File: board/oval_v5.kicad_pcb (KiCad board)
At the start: 2 copper layers, 100 x 60 mm, 143 parts, among them J1 HDR-5x1, J10 HDR-4x1, J11 HDR-4x1, J12 HDR-4x1, J13 HDR-4x1, J14 HDR-4x1, J15 HDR-4x1, J16 HDR-4x1, J17 HDR-4x1, J18 Conn_Coaxial, J19 Conn_01x02, J2 HDR-4x1, J20 Conn_01x02, J21 Conn_02x02_Counter_Clockwise, J22 HDR-2x1, J23 HDR-2x1, J25 Conn_01x06, J3 HDR-4x1, J4 Conn_01x06, J5 Micro_SD_Card, J6 Conn_01x02, J7 HDR-4x1, J8 Conn_01x08, J9 HDR-4x1, P1 USB_C_Plug_USB2.0, Q1 Q_PMOS_GSD, Q2 MMBT3904, Q3 MMBT3904, SW1 SW_DIP_x02, SW2 SW_DIP_x02, U1 RV-8803, U10 SiP32431DR3, U11 SiP32431DR3, U12 SiP32431DR3, U13 SiP32431DR3, U14 SiP32431DR3, U16 PCA9548APW, U17 SiP32431DR3, U18 PCA9555PW, U2 ESP32-S3-WROOM-1, U3 TMP117xxDRV, U4 RFM95W-915S2, U7 MAX3485, U8 AP7361C-33E, U9 AP7361C-33E

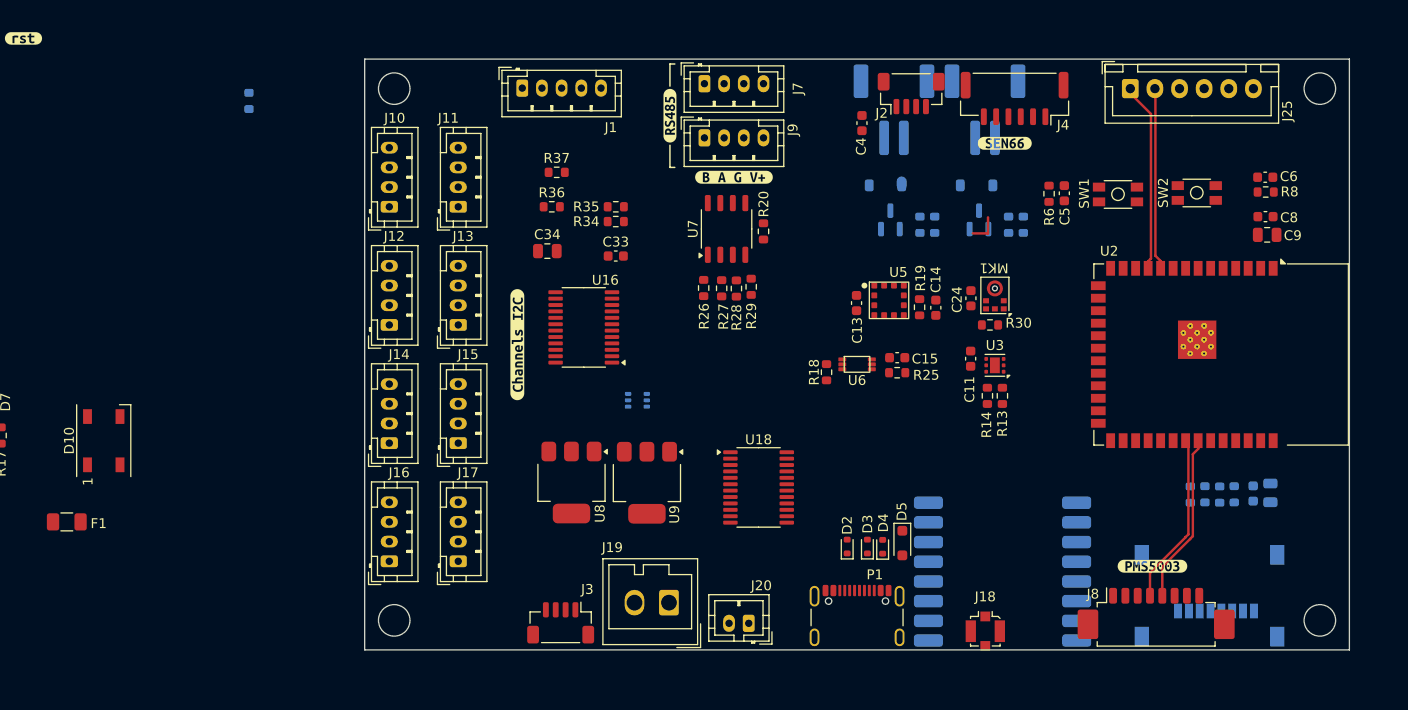
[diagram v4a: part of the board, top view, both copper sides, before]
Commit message: routing pads
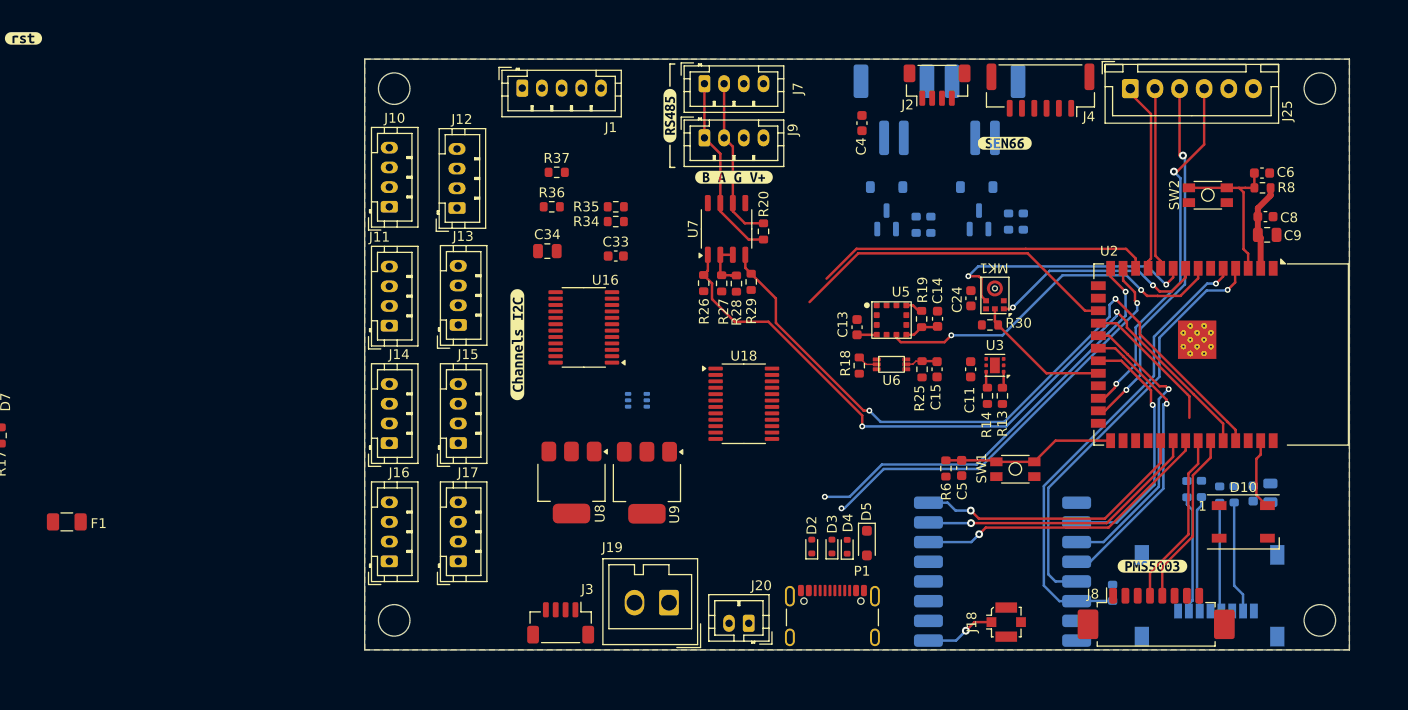
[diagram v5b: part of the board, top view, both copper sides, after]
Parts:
- moved D10 116.0 mm to (139.2, 97.0), turned to 0 degrees
- moved R12 100.9 mm to (126.0, 104.2)
- moved R6 29.8 mm to (109.0, 91.6)
- moved C5 29.8 mm to (110.6, 91.5)
- moved SW1 29.8 mm to (116.1, 91.7)
- moved J11 14.0 mm to (52.5, 77.1)
- moved J12 13.7 mm to (59.4, 65.1)
- moved U18 8.63 mm to (88.5, 85.0)
- moved C15 4.22 mm to (108.1, 81.5), turned to -90 degrees
- moved D2 3.60 mm to (95.4, 99.5)
- moved D3 3.60 mm to (97.5, 99.5)
- moved D4 3.60 mm to (99.0, 99.5)
- moved D5 3.60 mm to (101.0, 99.2)
- moved U6 3.50 mm to (103.5, 81.0)
- moved R18 3.39 mm to (100.2, 81.1)
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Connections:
- MK1 pad 1: WS_MIC -> MIC_WS
- MK1 pad 4: SCK_MIC -> MIC_SCK
- MK1 pad 6: SD_MIC -> MIC_SD
- R30 pad 1: SD_MIC -> MIC_SD
- U2 pad 24: rfm_dio1 -> GSM_RST
- U2 pad 25: rfm_dio2 -> GSM_PWRKEY
- U2 pad 31: rfm_dio0 -> rfm_dio2
- U2 pad 32: GSM_RST -> rfm_dio1
- U2 pad 33: PMS_Rx -> rfm_dio0
- U2 pad 34: PMS_Tx -> PMS_Rx
- U2 pad 35: GSM_PWRKEY -> PMS_Tx
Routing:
- net RS485_TX: track 0.00 -> 74.7 mm, vias 0 -> 2
- net RS485_RX: track 0.00 -> 72.2 mm, vias 0 -> 2
- net rfm_RST: track 0.00 -> 47.9 mm, vias 0 -> 1
- net USB_D+: track 0.00 -> 43.6 mm, vias 0 -> 2
- net rfm_CS: track 0.00 -> 43.3 mm, vias 0 -> 1
- net USB_D-: track 0.00 -> 43.2 mm, vias 0 -> 2
- net GSM_PWRKEY: track 0.00 -> 37.2 mm, vias 0 -> 2
- net GSM_RST: track 0.00 -> 37.0 mm, vias 0 -> 2
- net UV_SIG: track 0.00 -> 36.6 mm, vias 0 -> 2
- net SDA: track 1.92 -> 37.6 mm
- net SCL: track 1.99 -> 37.5 mm
- net rfm_dio0: track 0.00 -> 31.4 mm, vias 0 -> 1
- net SPI_MOSI: track 0.00 -> 30.4 mm, vias 0 -> 1
- net SPI_SCLK: track 0.00 -> 30.3 mm, vias 0 -> 1
- net rfm_dio1: track 0.00 -> 29.3 mm, vias 0 -> 1
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- added copper zone on B.Cu, net GND
- added copper zone on F.Cu, net GND

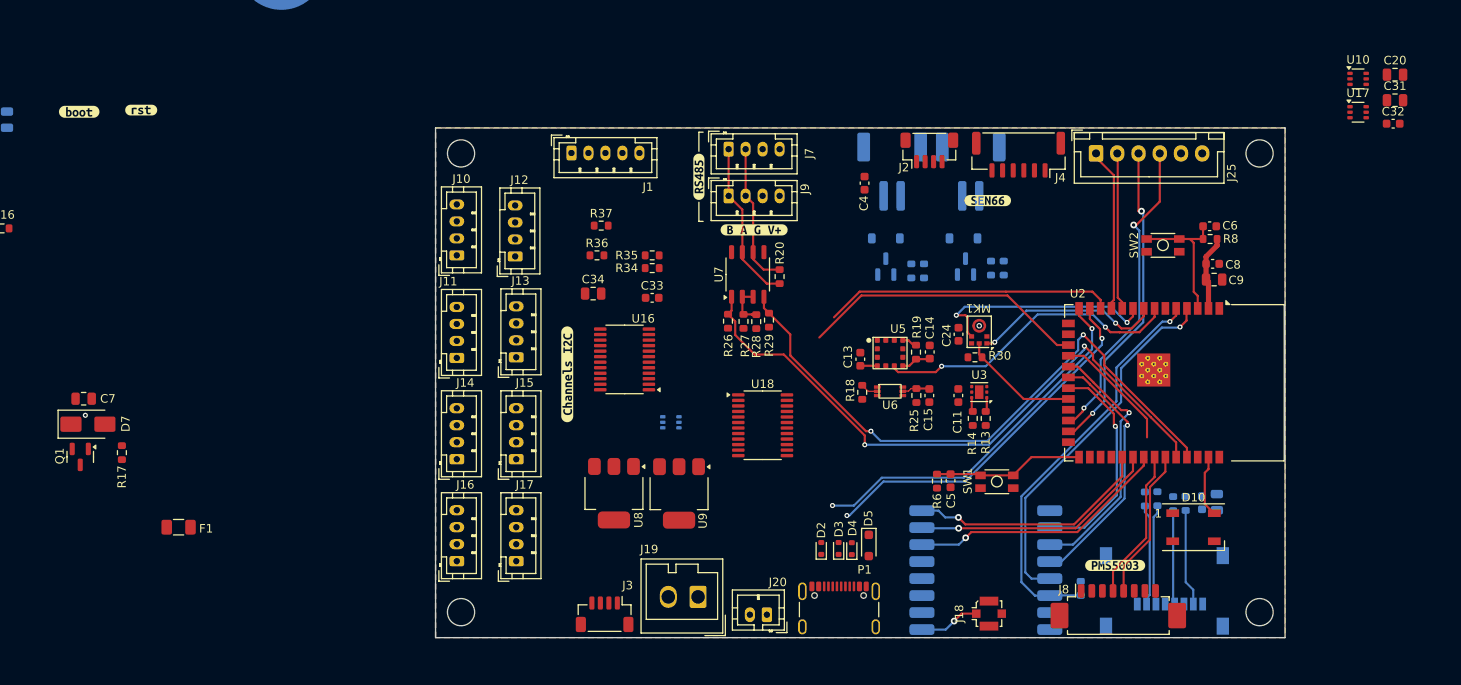
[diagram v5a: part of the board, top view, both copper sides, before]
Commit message: i2c multiplexer routed
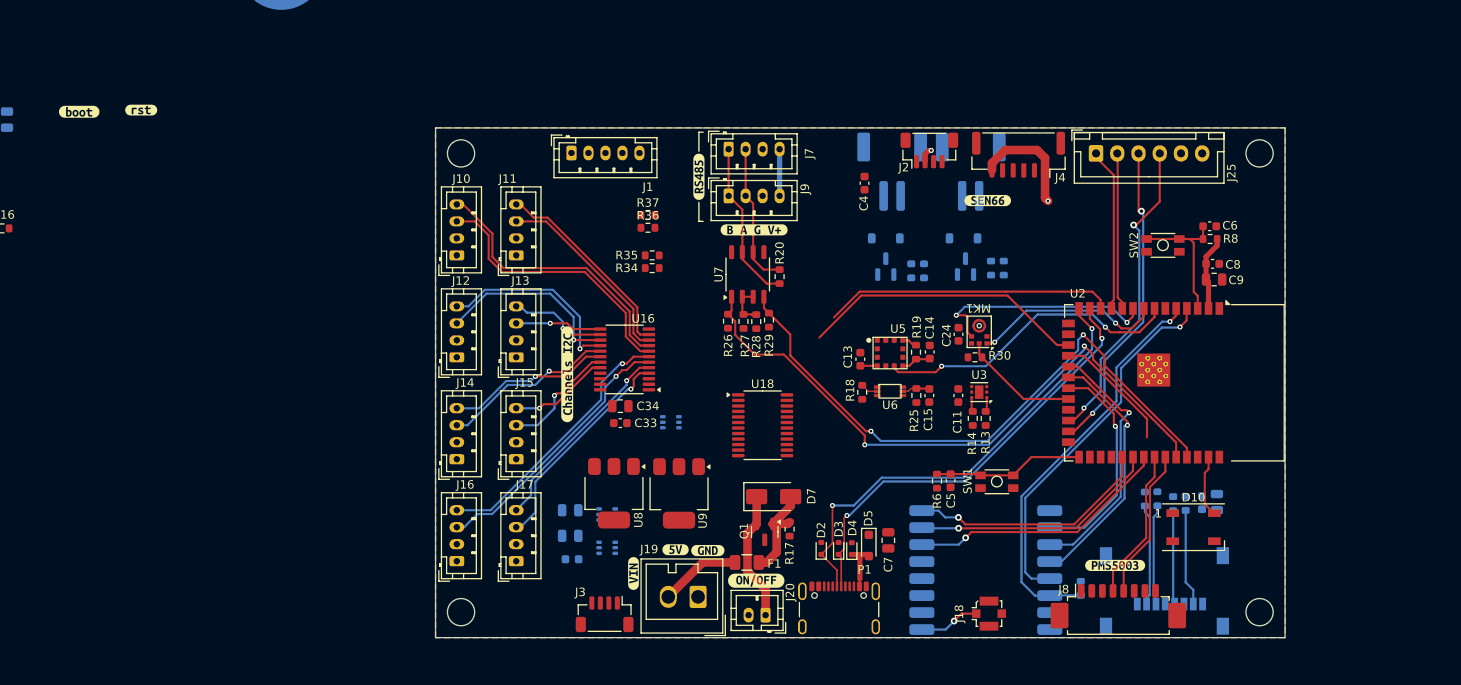
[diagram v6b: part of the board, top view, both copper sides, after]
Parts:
- added kibuzzard-69B0484A: G***, kibuzzard-69B0484A, F.Cu at (73.3, 102.5)
- added kibuzzard-69B0485B: G***, kibuzzard-69B0485B, F.Cu at (78.2, 99.7)
- added kibuzzard-69B0486A: G***, kibuzzard-69B0486A, F.Cu at (82.0, 99.8)
- added kibuzzard-69B04879: G***, kibuzzard-69B04879, F.Cu at (87.8, 103.3)
- C20, C31, C32, U10, U17: moved to B.Cu
- moved C20 109.8 mm to (65.8, 95.0), turned to 180 degrees
- moved C31 109.8 mm to (65.8, 98.0), turned to 180 degrees
- moved C32 109.4 mm to (66.1, 100.8), turned to 180 degrees
- moved U10 102.2 mm to (70.2, 95.5), turned to 180 degrees
- moved U17 102.2 mm to (70.2, 99.4), turned to 180 degrees
- moved C7 96.2 mm to (103.3, 98.5), turned to 90 degrees
- moved D7 81.2 mm to (89.8, 93.4)
- moved Q1 81.1 mm to (88.8, 97.5)
- moved R17 79.1 mm to (91.7, 97.2)
- moved F1 67.0 mm to (86.7, 101.2)
- moved C33 15.2 mm to (71.8, 84.8)
- moved J11 14.0 mm to (59.5, 65.0)
- moved J12 13.7 mm to (52.5, 77.0)
- moved C34 13.6 mm to (71.8, 82.8)
- moved R36 6.82 mm to (75.0, 61.8)
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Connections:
- J10 pad 3: SDA_0 -> SDA_2
- J10 pad 4: SCL_0 -> SCL_2
- J11 pad 3: SDA_2 -> SDA_3
- J11 pad 4: SCL_2 -> SCL_3
- J12 pad 3: SDA_4 -> SDA_5
- J12 pad 4: SCL_4 -> SCL_5
- J13 pad 3: SDA_6 -> SDA_4
- J13 pad 4: SCL_6 -> SCL_4
- J14 pad 3: SDA_1 -> SDA_6
- J14 pad 4: SCL_1 -> SCL_6
- J15 pad 3: SDA_3 -> SDA_7
- J15 pad 4: SCL_3 -> SCL_7
- J16 pad 3: SDA_5 -> SDA_1
- J16 pad 4: SCL_5 -> SCL_1
- J17 pad 3: SDA_7 -> SDA_0
- J17 pad 4: SCL_7 -> SCL_0
- R31 pad 2: Net-(U16-~{RESET}) -> I2C_BUS_RST
- U16 pad 3: Net-(U16-~{RESET}) -> I2C_BUS_RST
- U18 pad 15: unconnected-(U18-IO1_2-Pad15) -> I2C_BUS_RST
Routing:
- net V_S2: track 0.00 -> 193.2 mm, vias 0 -> 2
- net SCL_2: track 0.00 -> 32.7 mm
- net SDA_2: track 0.00 -> 32.2 mm
- net SDA_1: track 0.00 -> 31.6 mm, vias 0 -> 1
- net SCL_1: track 0.00 -> 31.3 mm, vias 0 -> 1
- net SDA_0: track 0.00 -> 25.7 mm, vias 0 -> 1
- net SCL_0: track 0.00 -> 23.9 mm, vias 0 -> 1
- net SCL_3: track 0.00 -> 23.7 mm
- net SDA_3: track 0.00 -> 23.1 mm
- net SDA_5: track 0.00 -> 22.9 mm, vias 0 -> 1
- net SCL_5: track 0.00 -> 22.9 mm, vias 0 -> 1
- net SDA_6: track 0.00 -> 20.6 mm, vias 0 -> 1
- net SCL_6: track 0.00 -> 19.4 mm, vias 0 -> 1
- net 5V_VDD: track 0.16 -> 15.3 mm, vias 1 -> 0
- net SDA_7: track 0.00 -> 13.8 mm, vias 0 -> 1
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- added copper zone on In1.Cu, net GND
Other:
- copper layers 2 -> 4

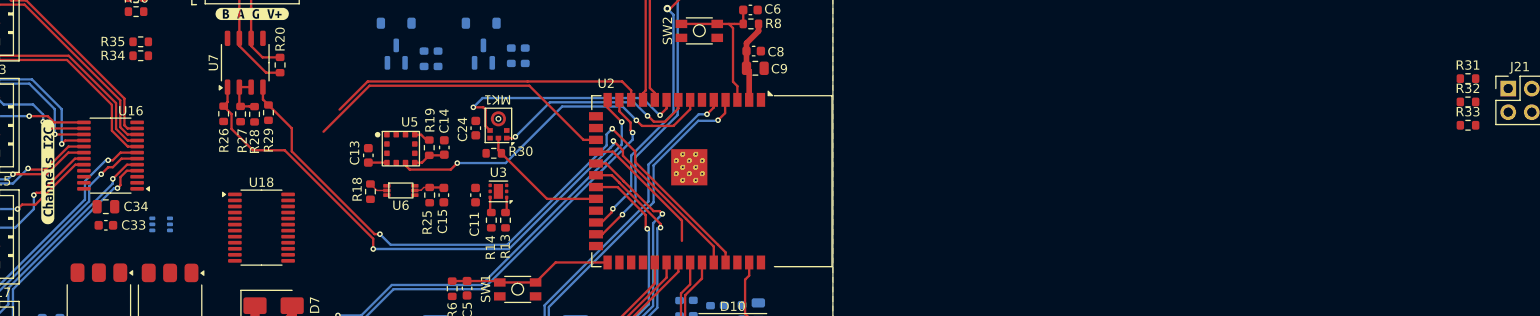
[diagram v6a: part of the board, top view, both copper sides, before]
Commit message: i2c adding pull up resistors
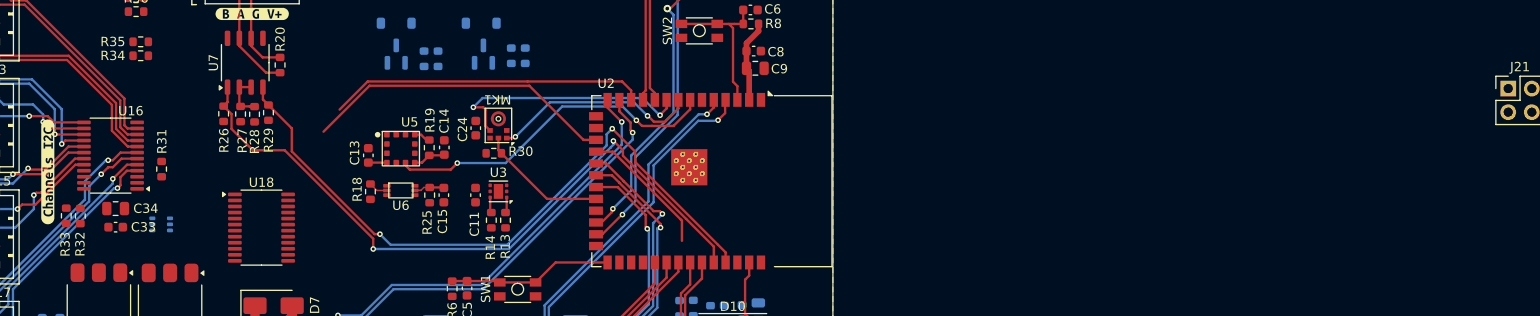
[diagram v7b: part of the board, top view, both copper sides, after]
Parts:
- moved R33 151.2 mm to (67.5, 83.7), turned to -90 degrees
- moved R32 149.9 mm to (69.0, 83.8), turned to -90 degrees
- moved R31 140.9 mm to (77.8, 78.7), turned to -90 degrees
- moved C33 1.07 mm to (72.8, 85.0)
- moved C34 1.07 mm to (72.8, 83.0)

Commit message: adding work in layout
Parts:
- added R38: 10k, Resistor_SMD:R_0603_1608Metric, F.Cu at (193.2, 69.5)
- added R39: 10k, Resistor_SMD:R_0603_1608Metric, F.Cu at (193.2, 71.0)
- added R40: 10k, Resistor_SMD:R_0603_1608Metric, F.Cu at (198.5, 80.9)
- added R41: 10k, Resistor_SMD:R_0603_1608Metric, F.Cu at (198.5, 83.4)
- added R42: 10k, Resistor_SMD:R_0603_1608Metric, F.Cu at (198.5, 85.9)
- added R43: 10k, Resistor_SMD:R_0603_1608Metric, F.Cu at (198.5, 88.4)
- added R44: 10k, Resistor_SMD:R_0603_1608Metric, F.Cu at (202.5, 75.8)
- added R45: 10k, Resistor_SMD:R_0603_1608Metric, F.Cu at (202.5, 78.4)
- added R46: 10k, Resistor_SMD:R_0603_1608Metric, F.Cu at (202.5, 80.9)
- added R47: 10k, Resistor_SMD:R_0603_1608Metric, F.Cu at (202.5, 83.4)
- added R48: 10k, Resistor_SMD:R_0603_1608Metric, F.Cu at (202.5, 85.9)
- added R49: 10k, Resistor_SMD:R_0603_1608Metric, F.Cu at (202.5, 88.4)
- added R50: 10k, Resistor_SMD:R_0603_1608Metric, F.Cu at (206.5, 75.8)
- added R51: 10k, Resistor_SMD:R_0603_1608Metric, F.Cu at (206.5, 78.4)
- added R52: 10k, Resistor_SMD:R_0603_1608Metric, F.Cu at (206.5, 80.9)
- added R53: 10k, Resistor_SMD:R_0603_1608Metric, F.Cu at (206.5, 83.4)
- R16, R17, R31, R32, R33, R36, R37, R6, R8: value 10K -> 10k
